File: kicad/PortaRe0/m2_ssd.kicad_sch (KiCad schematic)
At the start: 10 parts, among them CN1 M.2, U16 RT9080-33GJ5

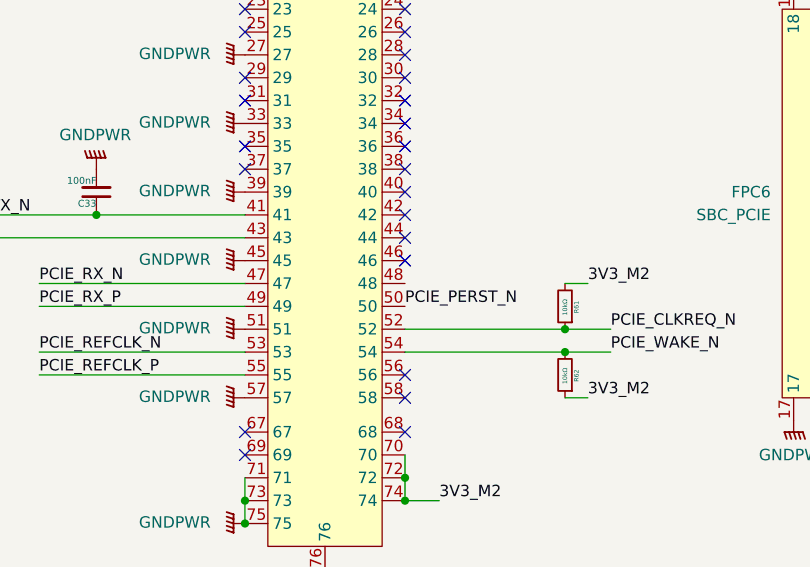
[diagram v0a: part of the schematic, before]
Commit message: Docs: session32終了処理・ドキュメント構成整理・session_close.py作成
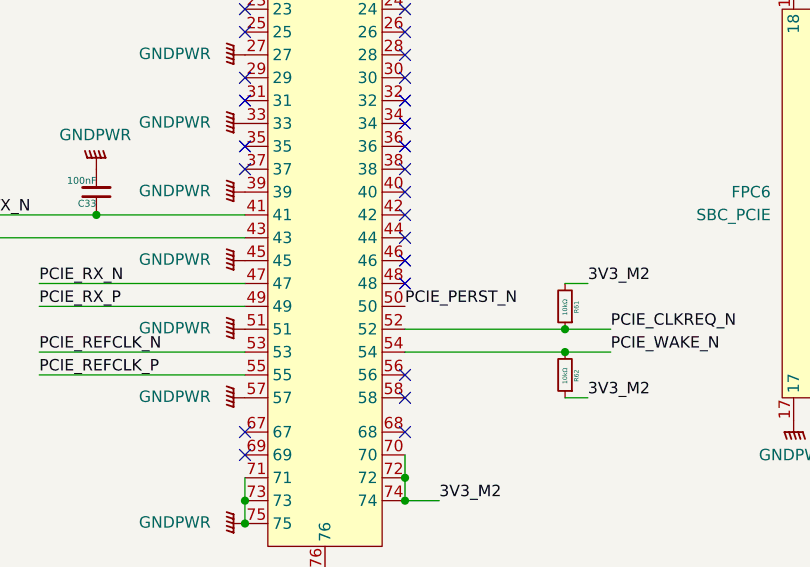
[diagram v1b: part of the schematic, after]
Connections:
- no-connect marks 38 -> 39
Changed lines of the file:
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@@
 		(at 153.67 106.68)
+	)
+	(no_connect
+		(at 101.6 101.6)
 	)
 	(wire

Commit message: Docs: session34終了処理・0402化確定・ディスプレイ調査・PCBレイアウト進行中
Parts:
- C21, C27, C29, C31, C33: footprint Capacitor_SMD:C_0603_1608Metric -> Capacitor_SMD:C_0402_1005Metric
- R61, R62: footprint Resistor_SMD:R_0603_1608Metric -> Resistor_SMD:R_0402_1005Metric
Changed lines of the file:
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@@
 			)
 		)
-		(property "Footprint" "Capacitor_SMD:C_0603_1608Metric"
+		(property "Footprint" "Capacitor_SMD:C_0402_1005Metric"
 			(at 171.45 43.18 0)
 			(effects
@@
 			)
 		)
-		(property "Footprint" "Resistor_SMD:R_0603_1608Metric"
+		(property "Footprint" "Resistor_SMD:R_0402_1005Metric"
 			(at 119.38 111.76 0)
 			(effects
@@
 			)
 		)
-		(property "Footprint" "Capacitor_SMD:C_0603_1608Metric"
+		(property "Footprint" "Capacitor_SMD:C_0402_1005Metric"
 			(at 198.12 43.18 0)
 			(effects
@@
 			)
 		)
-		(property "Footprint" "Capacitor_SMD:C_0603_1608Metric"
+		(property "Footprint" "Capacitor_SMD:C_0402_1005Metric"
 			(at 48.26 93.98 0)
 			(effects
@@
 			)
 		)
-		(property "Footprint" "Resistor_SMD:R_0603_1608Metric"
+		(property "Footprint" "Resistor_SMD:R_0402_1005Metric"
 			(at 119.38 104.14 0)
 			(effects
@@
 			)
 		)
-		(property "Footprint" "Capacitor_SMD:C_0603_1608Metric"
+		(property "Footprint" "Capacitor_SMD:C_0402_1005Metric"
 			(at 203.2 43.18 0)
 			(effects
@@
 			)
 		)
-		(property "Footprint" "Capacitor_SMD:C_0603_1608Metric"
+		(property "Footprint" "Capacitor_SMD:C_0402_1005Metric"
 			(at 67.31 91.44 0)
 			(effects
